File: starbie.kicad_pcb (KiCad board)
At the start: 2 copper layers, 96.5 x 96 mm, 10 parts, among them J1 Conn_01x04_Pin, J2 Conn_01x08_Pin, J3 Conn_01x05_Pin, J4 Conn_01x02_Pin, SW1 SW_Push, SW2 SW_Push, U1 DHT11

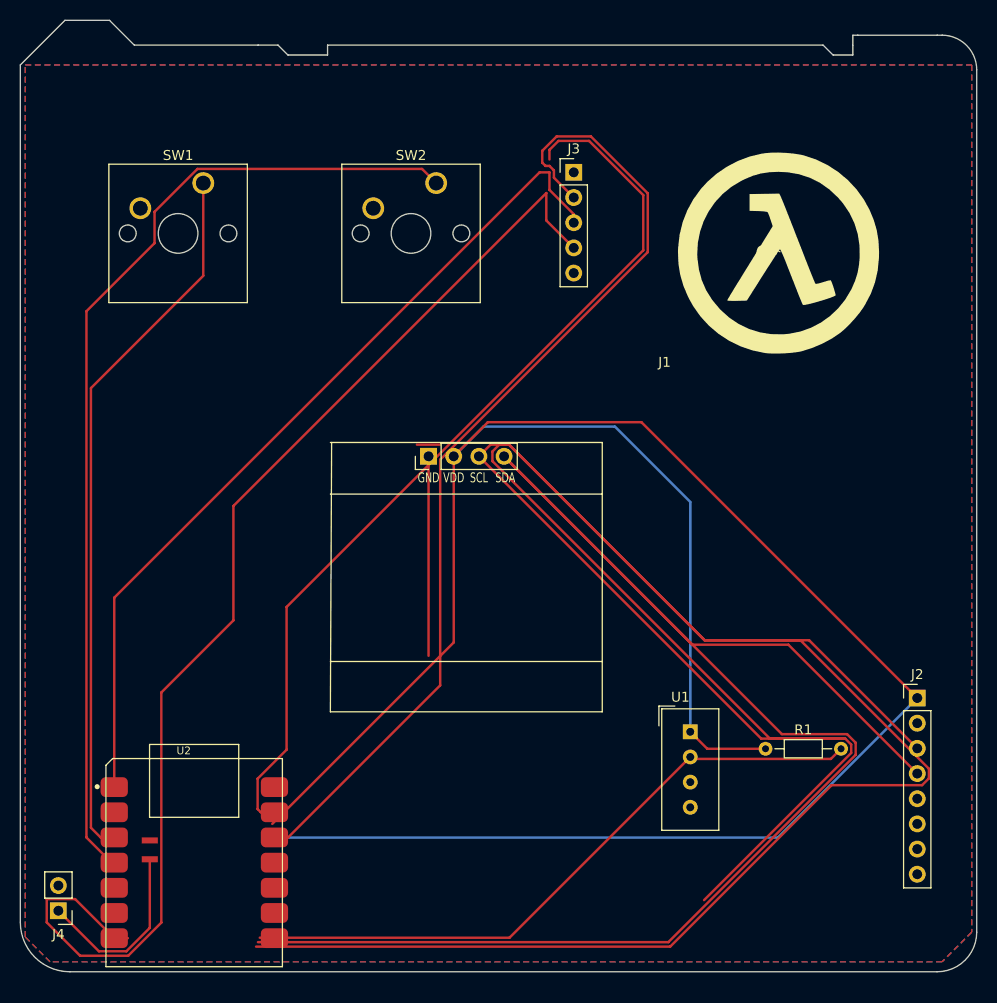
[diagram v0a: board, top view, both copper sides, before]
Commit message: Update Starbie schematic and PCB layout; add BOM CSV export.
Co-authored-by: Cursor <cursoragent@cursor.com>
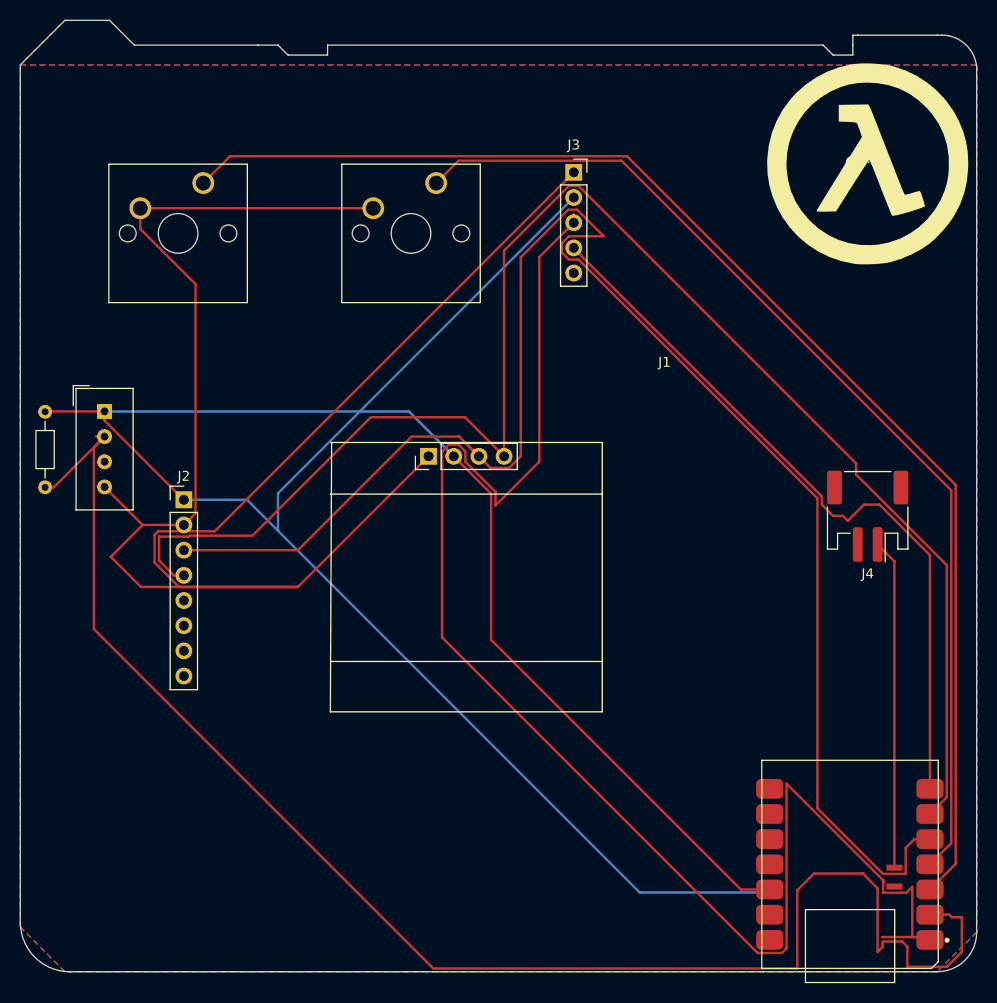
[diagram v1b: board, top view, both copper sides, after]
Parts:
- J3: footprint Connector_PinHeader_2.54mm:PinHeader_1x05_P2.54mm_Vertical -> Connector_PinSocket_2.54mm:PinSocket_1x05_P2.54mm_Vertical
- J4: footprint Connector_PinHeader_2.54mm:PinHeader_1x02_P2.54mm_Vertical -> Connector_JST:JST_PH_S2B-PH-SM4-TB_1x02-1MP_P2.00mm_Horizontal
- moved J4 90.8 mm to (116.5, 141.0)
- moved U2 86.5 mm to (123.6, 165.7), turned to 180 degrees
- moved R1 80.2 mm to (33.5, 130.5), turned to -90 degrees
- moved J2 76.7 mm to (47.5, 139.4)
- moved U1 67.4 mm to (39.5, 130.5)
- moved G*** 12.7 mm to (116.5, 105.5)
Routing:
- net /SCL: track 310.8 -> 163.6 mm
- net +3.3V: track 339.4 -> 235.9 mm
- net /DHT11 DATA: track 66.7 -> 158.0 mm
- net GND: track 113.1 -> 186.9 mm
- net /JOYSTICK_X: track 86.9 -> 154.3 mm
- net /GPI02: track 72.5 -> 132.7 mm
- net /JOYSTICK_Y: track 122.9 -> 74.2 mm
- net /BAT+: track 18.8 -> 33.3 mm
- net /SDA: track 171.8 -> 157.4 mm
- net /GPI03: track 100.6 -> 105.3 mm
